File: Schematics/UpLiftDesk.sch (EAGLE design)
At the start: 37 parts

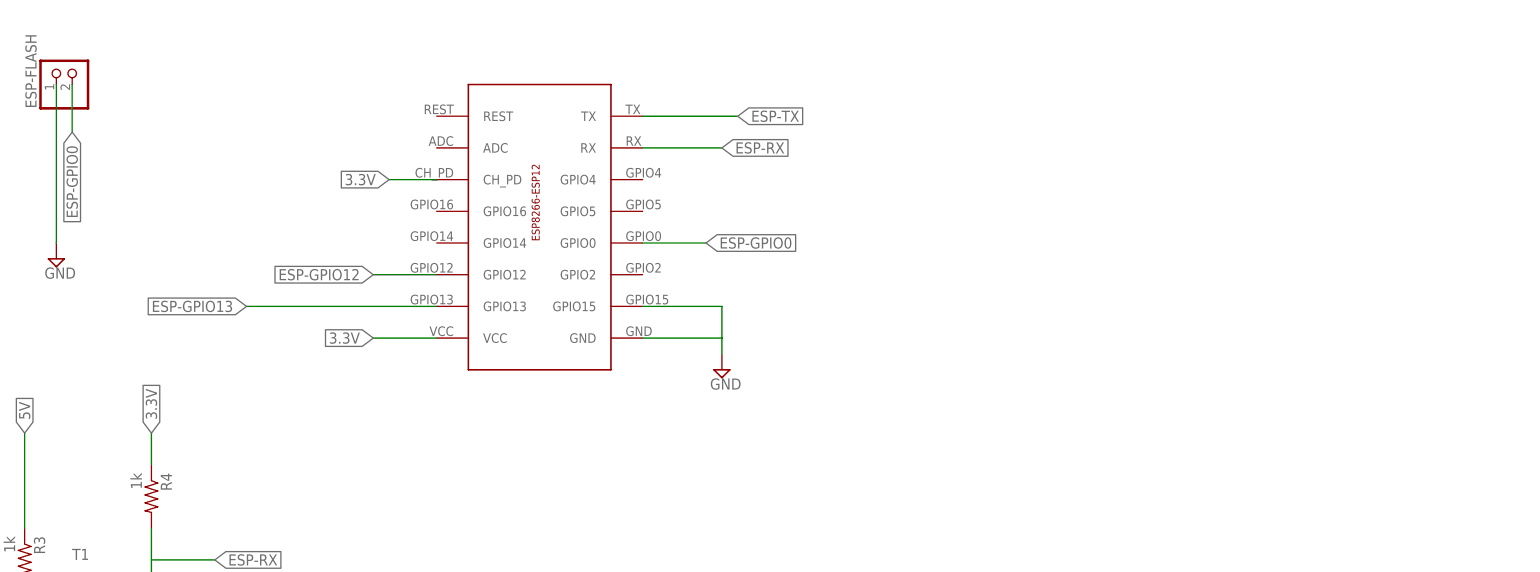
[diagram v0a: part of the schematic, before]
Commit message: Change ESP to through hole
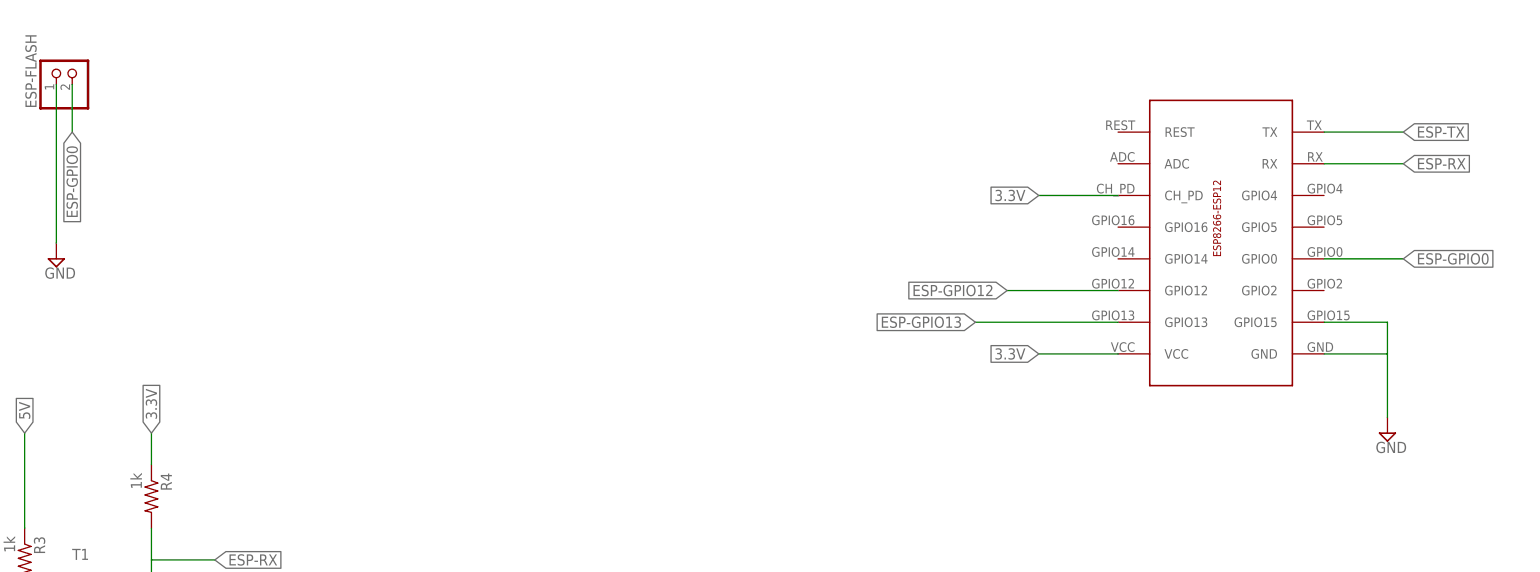
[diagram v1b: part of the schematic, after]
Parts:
- removed U$1: ESP-12, ESP8266:ESP-12
- added U$2: ESP-12-THROUGH, ESP8266:ESP-12-THROUGH
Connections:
- net 3.3V: now also U$2.CH_PD, U$2.VCC; no longer U$1.CH_PD, U$1.VCC
- net ESP-GPIO0: now also U$2.GPIO0; no longer U$1.GPIO0
- net ESP-GPIO12: now also U$2.GPIO12; no longer U$1.GPIO12
- net ESP-GPIO13: now also U$2.GPIO13; no longer U$1.GPIO13
- net ESP-RX: now also U$2.RX; no longer U$1.RX
- net ESP-TX: now also U$2.TX; no longer U$1.TX
- net GND: now also U$2.GND, U$2.GPIO15; no longer U$1.GND, U$1.GPIO15
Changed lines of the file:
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@@
 <part name="ESP-FLASH" library="pinhead" deviceset="PINHD-1X2" device=""/>
 <part name="SUPPLY6" library="supply2" deviceset="GND" device=""/>
-<part name="U$1" library="ESP8266" deviceset="ESP-12" device=""/>
 <part name="IC1" library="v-reg" deviceset="LM317TS" device=""/>
 <part name="C1" library="capacitor-wima" deviceset="C" device="2.5/2" value="0.1uf"/>
@@
 <part name="R8" library="resistor" deviceset="R-US_" device="0204/7" value="680"/>
 <part name="SUPPLY9" library="supply2" deviceset="GND" device=""/>
-<part name="SUPPLY10" library="supply2" deviceset="GND" device=""/>
 <part name="JP1" library="pinhead" deviceset="PINHD-1X1" device=""/>
 <part name="JP2" library="pinhead" deviceset="PINHD-1X1" device=""/>
@@
 <part name="JP20" library="pinhead" deviceset="PINHD-1X1" device=""/>
 <part name="SUPPLY8" library="supply2" deviceset="GND" device=""/>
+<part name="U$2" library="ESP8266" deviceset="ESP-12-THROUGH" device=""/>
+<part name="SUPPLY1" library="supply2" deviceset="GND" device=""/>
 </parts>
 <sheets>
@@
 <instance part="ESP-FLASH" gate="G$1" x="127" y="142.24" rot="R90"/>
 <instance part="SUPPLY6" gate="GND" x="124.46" y="111.76"/>
-<instance part="U$1" gate="G$1" x="198.12" y="116.84"/>
 <instance part="IC1" gate="1" x="208.28" y="20.32"/>
 <instance part="C1" gate="G$1" x="195.58" y="5.08"/>
@@
 <instance part="R8" gate="G$1" x="218.44" y="12.7" rot="R270"/>
 <instance part="SUPPLY9" gate="GND" x="208.28" y="-20.32"/>
-<instance part="SUPPLY10" gate="GND" x="231.14" y="93.98"/>
 <instance part="JP1" gate="G$1" x="101.6" y="2.54" rot="R90"/>
 <instance part="JP2" gate="G$1" x="109.22" y="2.54" rot="R90"/>
@@
 <instance part="JP20" gate="G$1" x="0" y="43.18" rot="R90"/>
 <instance part="SUPPLY8" gate="GND" x="0" y="22.86"/>
+<instance part="U$2" gate="G$1" x="307.34" y="114.3"/>
+<instance part="SUPPLY1" gate="GND" x="337.82" y="83.82"/>
 </instances>
 <busses>
@@
 <net name="ESP-TX" class="0">
 <segment>
-<pinref part="U$1" gate="G$1" pin="TX"/>
-<wire x1="218.44" y1="134.62" x2="233.68" y2="134.62" width="0.1524" layer="91"/>
-<label x="233.68" y="134.62" size="1.778" layer="95" xref="yes"/>
-</segment>
-<segment>
 <pinref part="JP1" gate="G$1" pin="1"/>
 <wire x1="101.6" y1="0" x2="101.6" y2="-12.7" width="0.1524" layer="91"/>
@@
 <wire x1="7.62" y1="40.64" x2="7.62" y2="27.94" width="0.1524" layer="91"/>
 <label x="7.62" y="27.94" size="1.778" layer="95" rot="R270" xref="yes"/>
+</segment>
+<segment>
+<pinref part="U$2" gate="G$1" pin="TX"/>
+<wire x1="327.66" y1="132.08" x2="340.36" y2="132.08" width="0.1524" layer="91"/>
+<label x="340.36" y="132.08" size="1.778" layer="95" xref="yes"/>
 </segment>
 </net>
@@
 </segment>
 <segment>
-<pinref part="SUPPLY10" gate="GND" pin="GND"/>
-<pinref part="U$1" gate="G$1" pin="GND"/>
-<wire x1="218.44" y1="99.06" x2="231.14" y2="99.06" width="0.1524" layer="91"/>
-<pinref part="U$1" gate="G$1" pin="GPIO15"/>
-<wire x1="218.44" y1="104.14" x2="231.14" y2="104.14" width="0.1524" layer="91"/>
-<wire x1="231.14" y1="104.14" x2="231.14" y2="99.06" width="0.1524" layer="91"/>
-<wire x1="231.14" y1="99.06" x2="231.14" y2="96.52" width="0.1524" layer="91"/>
-</segment>
-<segment>
 <pinref part="JP8" gate="G$1" pin="1"/>
 <wire x1="154.94" y1="0" x2="154.94" y2="-15.24" width="0.1524" layer="91"/>
@@
 <wire x1="0" y1="40.64" x2="0" y2="25.4" width="0.1524" layer="91"/>
 <pinref part="SUPPLY8" gate="GND" pin="GND"/>
+</segment>
+<segment>
+<pinref part="U$2" gate="G$1" pin="GPIO15"/>
+<wire x1="327.66" y1="101.6" x2="337.82" y2="101.6" width="0.1524" layer="91"/>
+<wire x1="337.82" y1="101.6" x2="337.82" y2="96.52" width="0.1524" layer="91"/>
+<pinref part="U$2" gate="G$1" pin="GND"/>
+<wire x1="337.82" y1="96.52" x2="337.82" y2="86.36" width="0.1524" layer="91"/>
+<wire x1="327.66" y1="96.52" x2="337.82" y2="96.52" width="0.1524" layer="91"/>
+<pinref part="SUPPLY1" gate="GND" pin="GND"/>
 </segment>
 </net>
@@
 </segment>
 <segment>
-<pinref part="U$1" gate="G$1" pin="RX"/>
-<wire x1="218.44" y1="129.54" x2="231.14" y2="129.54" width="0.1524" layer="91"/>
-<label x="231.14" y="129.54" size="1.778" layer="95" xref="yes"/>
+<pinref part="U$2" gate="G$1" pin="RX"/>
+<wire x1="327.66" y1="127" x2="340.36" y2="127" width="0.1524" layer="91"/>
+<label x="340.36" y="127" size="1.778" layer="95" xref="yes"/>
 </segment>
 </net>
@@
 </segment>
 <segment>
-<pinref part="U$1" gate="G$1" pin="VCC"/>
-<wire x1="185.42" y1="99.06" x2="175.26" y2="99.06" width="0.1524" layer="91"/>
-<label x="175.26" y="99.06" size="1.778" layer="95" rot="R180" xref="yes"/>
-</segment>
-<segment>
-<pinref part="U$1" gate="G$1" pin="CH_PD"/>
-<wire x1="185.42" y1="124.46" x2="177.8" y2="124.46" width="0.1524" layer="91"/>
-<label x="177.8" y="124.46" size="1.778" layer="95" rot="R180" xref="yes"/>
+<pinref part="U$2" gate="G$1" pin="CH_PD"/>
+<wire x1="294.64" y1="121.92" x2="281.94" y2="121.92" width="0.1524" layer="91"/>
+<label x="281.94" y="121.92" size="1.778" layer="95" rot="R180" xref="yes"/>
+</segment>
+<segment>
+<pinref part="U$2" gate="G$1" pin="VCC"/>
+<wire x1="294.64" y1="96.52" x2="281.94" y2="96.52" width="0.1524" layer="91"/>
+<label x="281.94" y="96.52" size="1.778" layer="95" rot="R180" xref="yes"/>
 </segment>
 </net>
@@
 </segment>
 <segment>
-<pinref part="U$1" gate="G$1" pin="GPIO12"/>
-<wire x1="185.42" y1="109.22" x2="175.26" y2="109.22" width="0.1524" layer="91"/>
-<label x="175.26" y="109.22" size="1.778" layer="95" rot="R180" xref="yes"/>
+<pinref part="U$2" gate="G$1" pin="GPIO12"/>
+<wire x1="294.64" y1="106.68" x2="276.86" y2="106.68" width="0.1524" layer="91"/>
+<label x="276.86" y="106.68" size="1.778" layer="95" rot="R180" xref="yes"/>
 </segment>
 </net>
@@
 </segment>
 <segment>
-<pinref part="U$1" gate="G$1" pin="GPIO13"/>
-<wire x1="185.42" y1="104.14" x2="154.94" y2="104.14" width="0.1524" layer="91"/>
-<label x="154.94" y="104.14" size="1.778" layer="95" rot="R180" xref="yes"/>
+<pinref part="U$2" gate="G$1" pin="GPIO13"/>
+<wire x1="294.64" y1="101.6" x2="271.78" y2="101.6" width="0.1524" layer="91"/>
+<label x="271.78" y="101.6" size="1.778" layer="95" rot="R180" xref="yes"/>
 </segment>
 </net>
@@
 </segment>
 <segment>
-<pinref part="U$1" gate="G$1" pin="GPIO0"/>
-<wire x1="218.44" y1="114.3" x2="228.6" y2="114.3" width="0.1524" layer="91"/>
-<label x="228.6" y="114.3" size="1.778" layer="95" xref="yes"/>
-</segment>
-</net>
+<pinref part="U$2" gate="G$1" pin="GPIO0"/>
+<wire x1="327.66" y1="111.76" x2="340.36" y2="111.76" width="0.1524" layer="91"/>
+<label x="340.36" y="111.76" size="1.778" layer="95" xref="yes"/>
+</segment>
+</net>
